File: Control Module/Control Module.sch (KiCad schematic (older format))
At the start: 64 parts, among them J1 USB_B, SW1 SW_Push, U1 74LS161, U10 74LS30, U2 74LS173, U3 74LS273, U4 28C256, U5 28C256, U6 74LS08, U7 74LS04, U8 74LS02, U9 74LS02

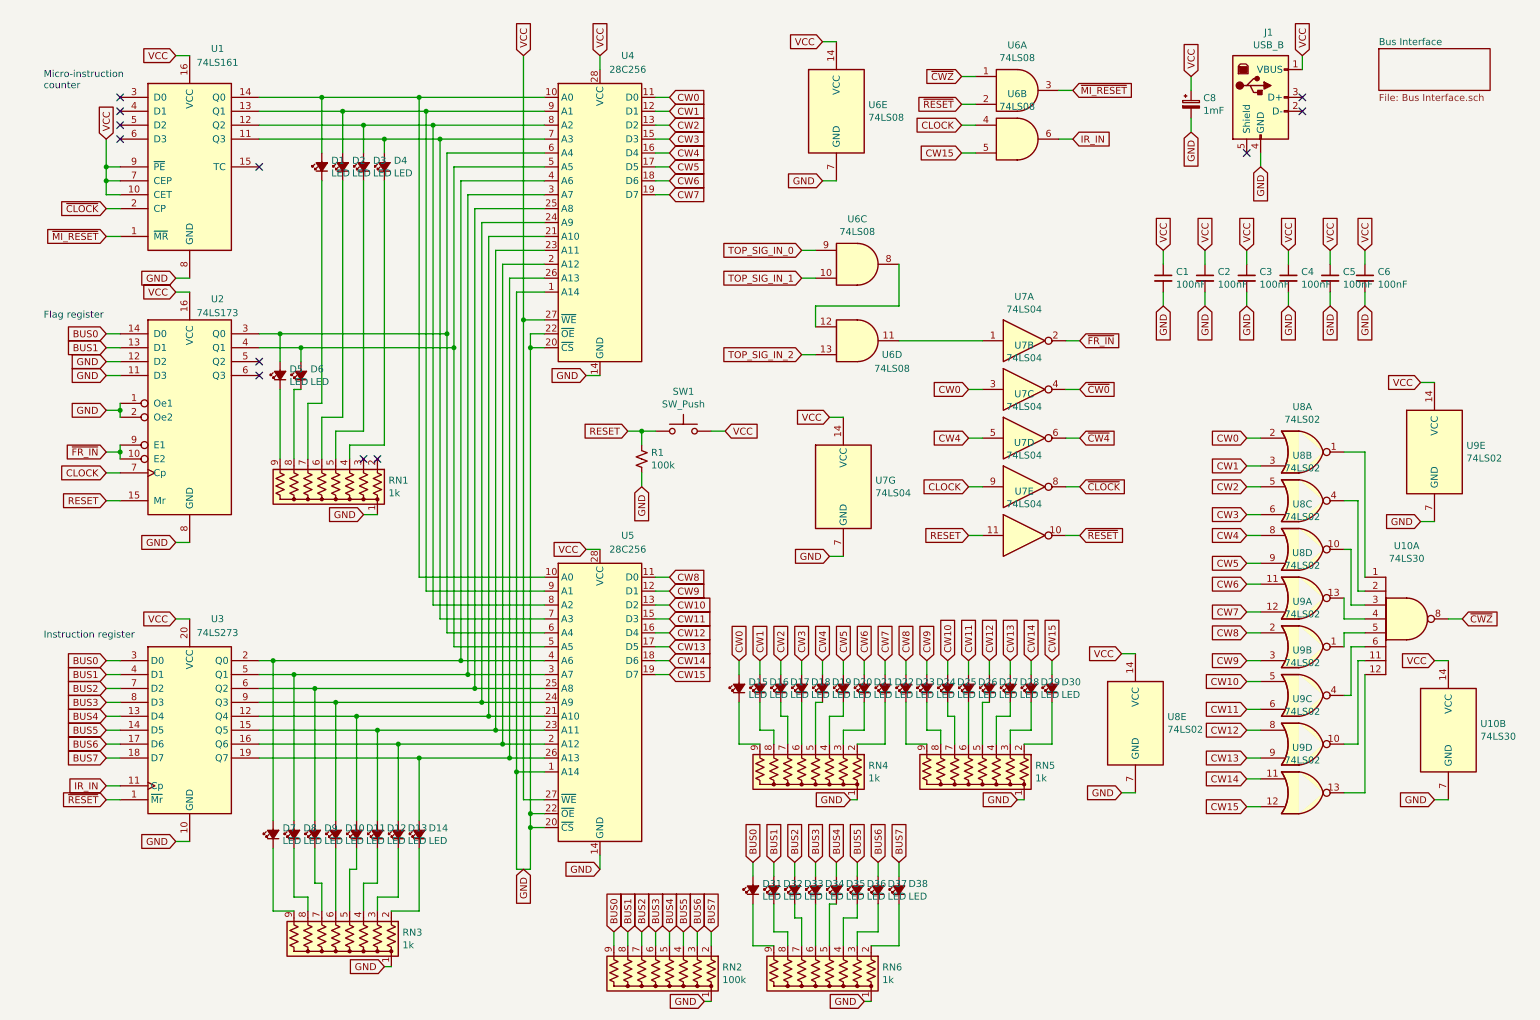
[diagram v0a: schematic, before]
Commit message: Fixed floating inputs; improved power; added parts list; replaced JK latches
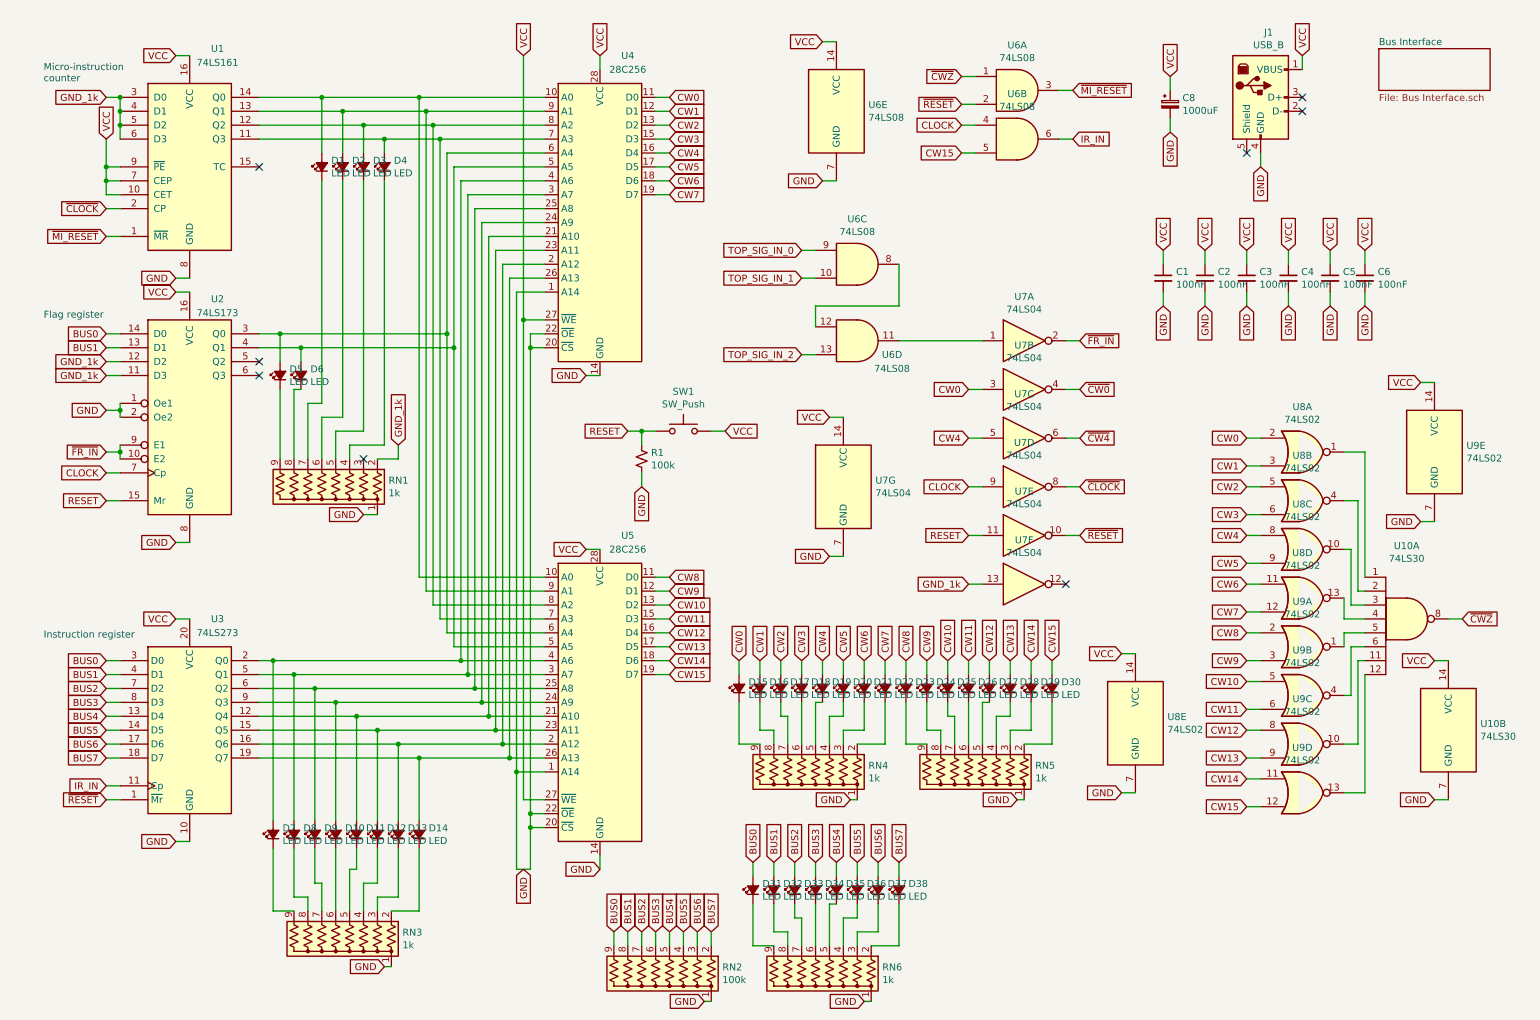
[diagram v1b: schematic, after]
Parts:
- added unit 6 of U7
- C8: value 1mF -> 1000uF
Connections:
- net GND: no longer U2.11 (D3), U2.12 (D2)
- net GND_1k: now reaches U1.3 (D0)
- net GND_1k: now also RN1.2 (R1), U1.4 (D1), U1.5 (D2), U1.6 (D3), U2.11 (D3), U2.12 (D2), U7.13
- no-connect marks 12 -> 8
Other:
- moved on the sheet: C8
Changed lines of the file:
@@
 Connection ~ 3400 1450
 NoConn ~ 2100 1650
-NoConn ~ 1100 1150
-NoConn ~ 1100 1250
-NoConn ~ 1100 1350
-NoConn ~ 1100 1450
 Text GLabel 1500 850  0    50   Input ~ 0
 VCC
@@
 Wire Wire Line
 	1500 2550 1600 2550
-Text Notes 550  1100 0    50   ~ 0
+Text Notes 550  1050 0    50   ~ 0
 Micro-instruction\ncounter
 Text Notes 550  2750 0    50   ~ 0
@@
 NoConn ~ 2100 3050
 NoConn ~ 2100 3150
-Text GLabel 1000 3050 0    50   Input ~ 0
-GND
 Wire Wire Line
 	1000 3050 1100 3050
-Text GLabel 1000 3150 0    50   Input ~ 0
-GND
 Wire Wire Line
 	1000 3150 1100 3150
@@
 	3000 1750 3000 3650
 NoConn ~ 2850 3750
-NoConn ~ 2950 3750
 Text GLabel 2850 4150 0    50   Input ~ 0
 GND
@@
 Wire Wire Line
 	10050 2350 10050 2250
-Text GLabel 8800 1000 1    50   Input ~ 0
+Text GLabel 8650 1000 1    50   Input ~ 0
 VCC
-Text GLabel 8800 1400 3    50   Input ~ 0
-GND
-Wire Wire Line
-	8800 1400 8800 1300
-Wire Wire Line
-	8800 1100 8800 1000
+Text GLabel 8650 1400 3    50   Input ~ 0
+GND
+Wire Wire Line
+	8650 1400 8650 1300
+Wire Wire Line
+	8650 1100 8650 1000
 $Comp
 L Device:CP_Small C8
 U 1 1 6643C54F
-P 8800 1200
-F 0 "C8" H 8888 1246 50  0000 L CNN
-F 1 "1mF" H 8888 1155 50  0000 L CNN
-F 2 "Capacitor_THT:CP_Radial_D8.0mm_P3.50mm" H 8800 1200 50  0001 C CNN
-F 3 "~" H 8800 1200 50  0001 C CNN
-	1    8800 1200
+P 8650 1200
+F 0 "C8" H 8738 1246 50  0000 L CNN
+F 1 "1000uF" H 8738 1155 50  0000 L CNN
+F 2 "Capacitor_THT:CP_Radial_D8.0mm_P3.50mm" H 8650 1200 50  0001 C CNN
+F 3 "~" H 8650 1200 50  0001 C CNN
+	1    8650 1200
 	1    0    0    -1
 $EndComp
@@
 Wire Wire Line
 	4850 3550 4950 3550
+Text GLabel 3100 3650 1    50   Input ~ 0
+GND_1k
+Wire Wire Line
+	2950 3750 3100 3750
+Wire Wire Line
+	3100 3750 3100 3650
+Text GLabel 1000 1150 0    50   Input ~ 0
+GND_1k
+Wire Wire Line
+	1000 1150 1100 1150
+Wire Wire Line
+	1100 1150 1100 1250
+Connection ~ 1100 1150
+Connection ~ 1100 1250
+Wire Wire Line
+	1100 1250 1100 1350
+Connection ~ 1100 1350
+Wire Wire Line
+	1100 1350 1100 1450
+Text GLabel 1000 3050 0    50   Input ~ 0
+GND_1k
+Text GLabel 1000 3150 0    50   Input ~ 0
+GND_1k
+$Comp
+L 74xx:74LS04 U7
+U 6 1 604A58E6
+P 7600 4650
+F 0 "U7" H 7600 4967 50  0000 C CNN
+F 1 "74LS04" H 7600 4876 50  0000 C CNN
+F 2 "Package_DIP:DIP-14_W7.62mm" H 7600 4650 50  0001 C CNN
+F 3 "http://www.ti.com/lit/gpn/sn74LS04" H 7600 4650 50  0001 C CNN
+	6    7600 4650
+	1    0    0    -1
+$EndComp
+NoConn ~ 7900 4650
+Text GLabel 7200 4650 0    50   Input ~ 0
+GND_1k
+Wire Wire Line
+	7200 4650 7300 4650
 $EndSCHEMATC

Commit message: Revise control and RAM modules
- Change control signals on low going clock
- Pull down control signals with 1k resistors
- AND the write signal with clock on RAM / ROM module
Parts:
- added RN7, RN8: 1k, Resistor_THT:R_Array_SIP9, symbol Device:R_Network08_US
- R1, RN2: value 100k -> 1k
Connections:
- net CLOCK: no longer U2.7 (Cp), U6.4
- net CW0: now also RN7.9 (R8)
- net CW1: now also RN7.8 (R7)
- net CW10: now also RN8.7 (R6)
- net CW11: now also RN8.6 (R5)
- net CW12: now also RN8.5 (R4)
- net CW13: now also RN8.4 (R3)
- net CW14: now also RN8.3 (R2)
- net CW15: now also RN8.2 (R1)
- net CW2: now also RN7.7 (R6)
- net CW3: now also RN7.6 (R5)
- net CW4: now also RN7.5 (R4)
- net CW5: now also RN7.4 (R3)
- net CW6: now also RN7.3 (R2)
- net CW7: now also RN7.2 (R1)
- net CW8: now also RN8.9 (R8)
- net CW9: now also RN8.8 (R7)
- net GND: now also RN7.1 (common), RN8.1 (common)
- net VCC: no longer U1.9 (~PE)
- net ~CLOCK: now also U2.7 (Cp), U6.1, U6.2, U6.4; no longer U1.2 (CP)
- net ~CWZ: now also U1.9 (~PE); no longer U6.1
- net ~RESET: now also U1.1 (~MR); no longer U6.2
- net ~MI_RESET renamed MI_CLOCK
- net MI_CLOCK: now also U1.2 (CP); no longer U1.1 (~MR)
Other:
- note added: "MI_CLOCK is buffered to add a tiny delay, to ensure\nIR_IN goes high before the EEPROM signals invalidate."
- moved on the sheet: C1, C2, C3, C4, C5, C6, D31, D32, D33, D34, D35, D36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

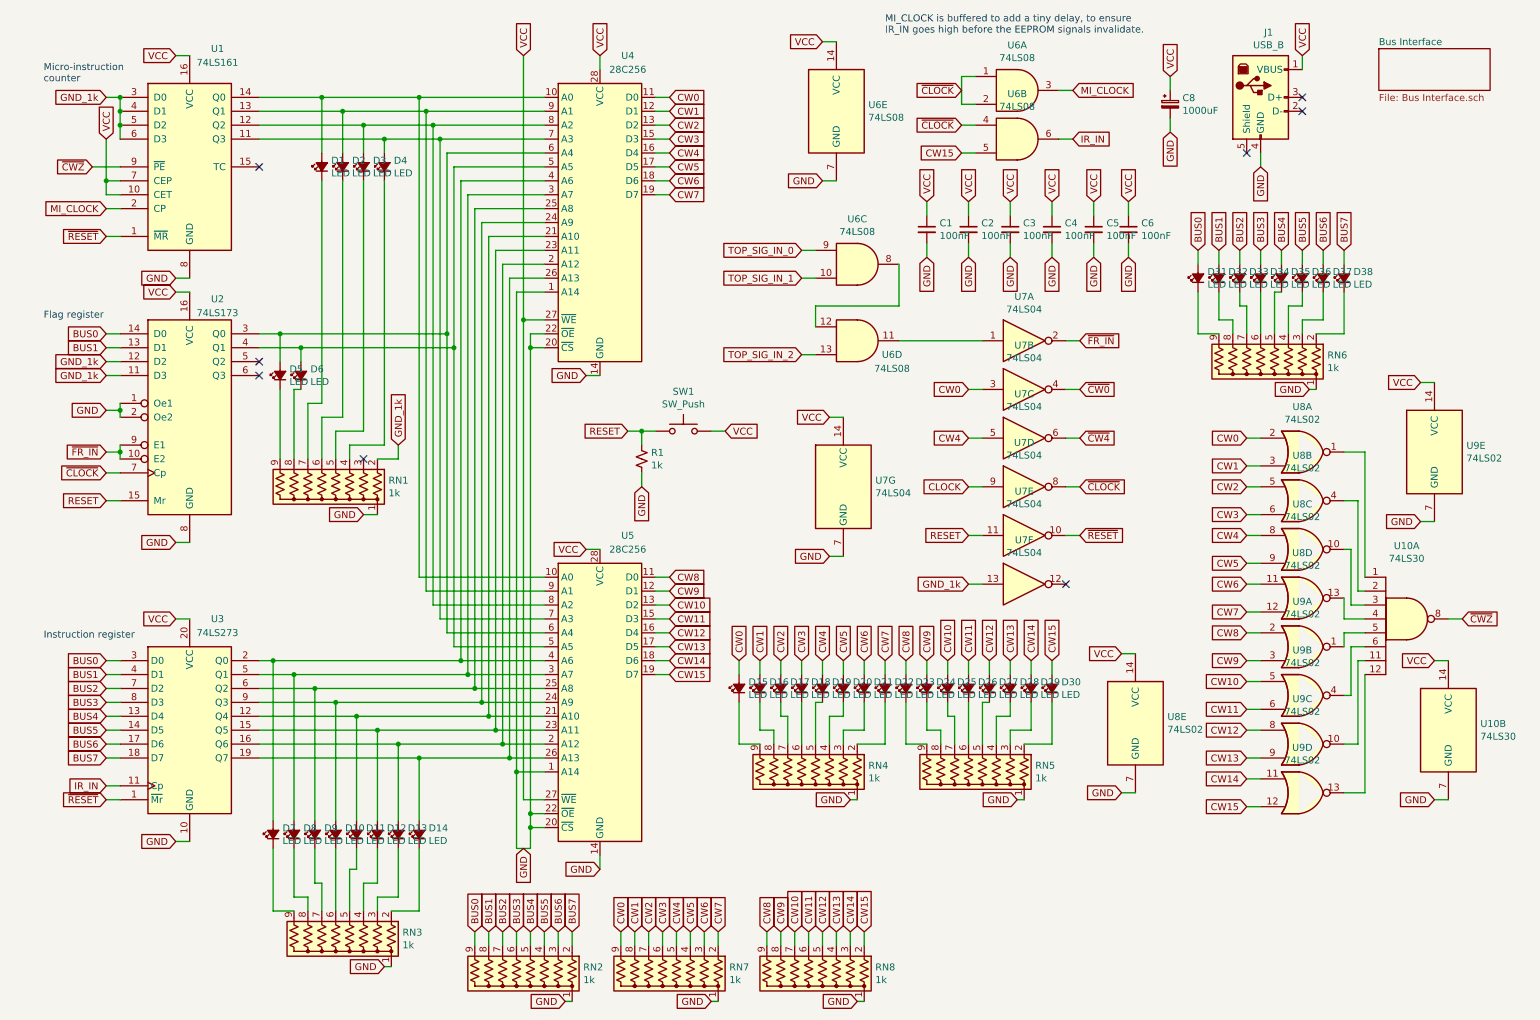
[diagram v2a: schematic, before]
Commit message: Control module sch: remove auto-MI reset; remove control line pull-downs; instruction register, 273 -> 2x173
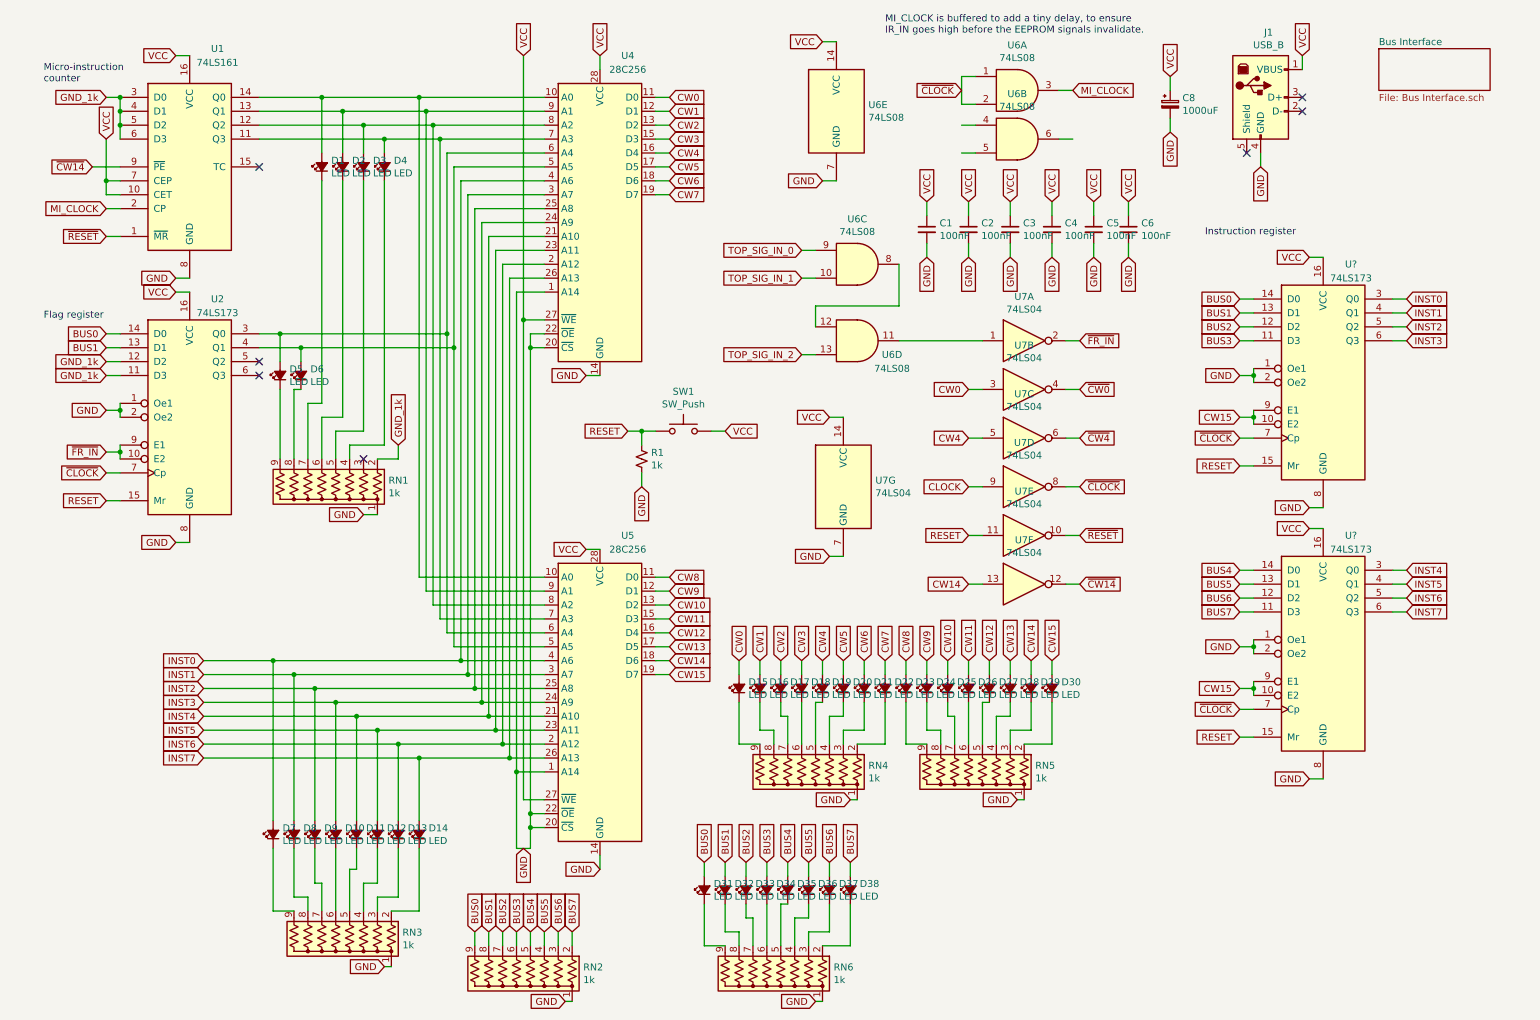
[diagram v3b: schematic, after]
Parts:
- removed RN7, RN8: 1k, Resistor_THT:R_Array_SIP9, symbol Device:R_Network08_US
- removed U10: 74LS30, Package_DIP:DIP-14_W7.62mm, symbol 74xx:74LS30
- removed U3: 74LS273, Package_DIP:DIP-20_W7.62mm, symbol 74xx:74LS273
- removed U8, U9: 74LS02, Package_DIP:DIP-14_W7.62mm, symbol 74xx:74LS02
- added U? (x2): 74LS173, Package_DIP:DIP-16_W7.62mm, symbol 74xx:74LS173
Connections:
- net ~CWZ is gone; now on net ~CW14: U1.9 (~PE)
- net BUS0: now also U?.14 (D0)
- net BUS1: now also U?.13 (D1)
- net BUS2: now also U?.12 (D2)
- net BUS3: now also U?.11 (D3)
- net BUS4: now also U?.14 (D0)
- net BUS5: now also U?.13 (D1)
- net BUS6: now also U?.12 (D2)
- net BUS7: now also U?.11 (D3)
- net CW14: now also U7.13
- net CW15: now also U?.10 (E2), U?.10 (E2), U?.9 (E1), U?.9 (E1); no longer U6.5
- net GND: now also U?.1 (Oe1), U?.1 (Oe1), U?.2 (Oe2), U?.2 (Oe2), U?.8 (GND), U?.8 (GND)
- net GND_1k: no longer U7.13
- net RESET: now also U?.15 (Mr), U?.15 (Mr)
- net VCC: now also U?.16 (VCC), U?.16 (VCC)
- net ~CLOCK: now also U?.7 (Cp), U?.7 (Cp); no longer U6.4
- net INST6: now reaches D13.2 (A), U4.2 (A12), U5.2 (A12)
- net INST6: now also U?.5 (Q2)
- net INST4: now reaches D11.2 (A), U4.21 (A10), U5.21 (A10)
- net INST4: now also U?.3 (Q0)
- net INST5: now reaches D12.2 (A), U4.23 (A11), U5.23 (A11)
- net INST5: now also U?.4 (Q1)
- net INST3: now reaches D10.2 (A), U4.24 (A9), U5.24 (A9)
- net INST3: now also U?.6 (Q3)
- net INST2: now reaches D9.2 (A), U4.25 (A8), U5.25 (A8)
- net INST2: now also U?.5 (Q2)
- net INST7: now reaches D14.2 (A), U4.26 (A13), U5.26 (A13)
- net INST7: now also U?.6 (Q3)
- net INST1: now reaches D8.2 (A), U4.3 (A7), U5.3 (A7)
- net INST1: now also U?.4 (Q1)
- net INST0: now reaches D7.2 (A), U4.4 (A6), U5.4 (A6)
- net INST0: now also U?.3 (Q0)
- net ~CW14: now reaches U7.12
- net IR_IN: no longer names the net of U6.6
- no-connect marks 8 -> 7
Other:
- moved on the sheet: D31, D32, D33, D34, D35, D36, D37, D38, RN6

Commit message: Update all boards to r3, and update revision log and gitignore
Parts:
- C8: symbol Device:CP_Small -> Control~Module-rescue:CP_Small-Device
- D1, D10, D11, D12, D13, D14, D15, D16, D17, D18, D19, D2, D20, D21, D22, D23, D24, D25, D26, D27, D28, D29, D3, D30, D31, D32, D33, D34, D35, D36, D37, D38, D4, D5, D6, D7, D8, D9: symbol Device:LED_Small_ALT -> Control~Module-rescue:LED_Small_ALT-Device
- gave numbers to parts that had none: 2
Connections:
- net labels added: ~{CLOCK}, ~{CW0}, ~{CW14}, ~{CW4}, ~{FR_IN}, ~{RESET}
- net labels removed: ~CLOCK, ~CW0, ~CW14, ~CW4, ~FR_IN, ~RESET
- no-connect marks 7 -> 8
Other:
- note added: "MI_CLOCK is buffered to add a tiny delay, to ensure instruction\nand flags registers input before the EEPROM signals invalidate."
- note removed: "MI_CLOCK is buffered to add a tiny delay, to ensure\nIR_IN goes high before the EEPROM signals invalidate."
- moved on the sheet: RN4, RN5
